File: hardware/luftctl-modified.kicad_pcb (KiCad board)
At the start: 2 copper layers, 56.6 x 43 mm, 45 parts, among them J1 USB_C_Receptacle_USB2.0, J2 UART, J3 I2C, J4 PWM Fan, J5 PWM Fan, J6 Conn_01x08, SW1 Reset, U3 USBLC6-4SC6, U4 ESP32-C3-WROOM-02, U5 CH224K, U6 LMR51420YFDDCR

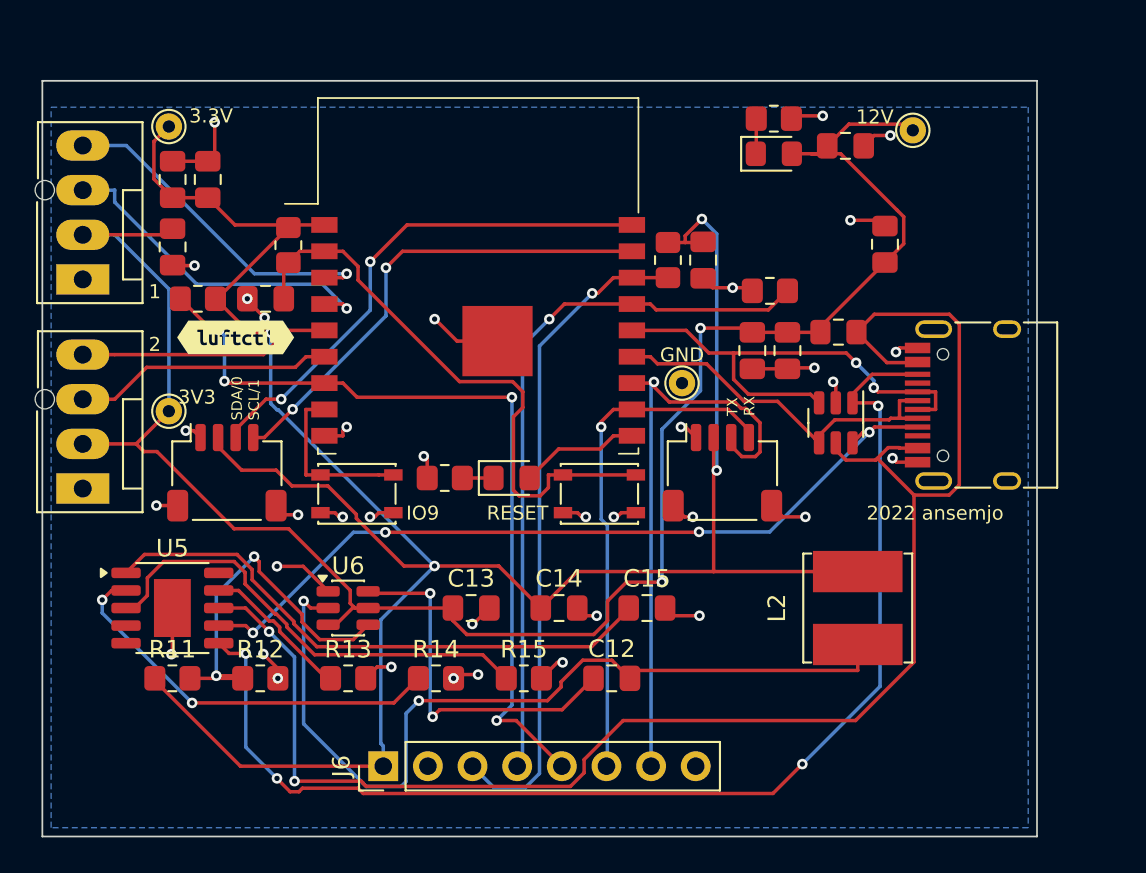
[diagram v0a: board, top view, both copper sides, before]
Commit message: CH224K: fix 12V CFG straps + VDD supply per datasheet; re-route
Datasheet research (WCH CH224 V2.0; TI LMR51420 SLUSEF6C), cross-verified,
corrected two bugs in the CH224K PD-trigger wiring that would have made the
board negotiate 9V with an unpowered controller:

- CFG3 must be pulled HIGH (to VDD) for 12V, not strapped to GND. CH224K has no
  internal CFG pull-ups, so R15 is changed from a 0R GND strap to a 10k pull-up
  to VDD (R15/CFG3 -> VDD_CH). CFG1/CFG2 stay strapped to GND (R13/R14 = 0R):
  CFG1,CFG2,CFG3 = 0,0,1 = 12V.
- VDD (pin 1) needs a series feed from VBUS; add R16 = 1k (VBUS -> VDD_CH) with
  the existing C15 1uF bypass. Previously VDD only had the cap (never powered).

LMR51420 3.3V buck confirmed correct as-is: VREF = 0.6V, R11/R12 = 100k/22k ->
3.327V (in tolerance; TI's exact pair is 100k/22.1k), no feedforward cap.

Board re-synced and re-routed with the corrections (0 unrouted, 0 clearance
violations; remaining DRC items are pre-existing footprint/silk/test-point
issues from the original board). Stale "5V" connector silk corrected to 3V3.
Assembly BOM/CPL and gerbers regenerated (19/27 lines with in-stock LCSC; new
R16 1k = C6654733). Datasheet-confirmed values documented in MODIFICATIONS.md.

Co-Authored-By: Claude Opus 4.8 (1M context) <noreply@anthropic.com>
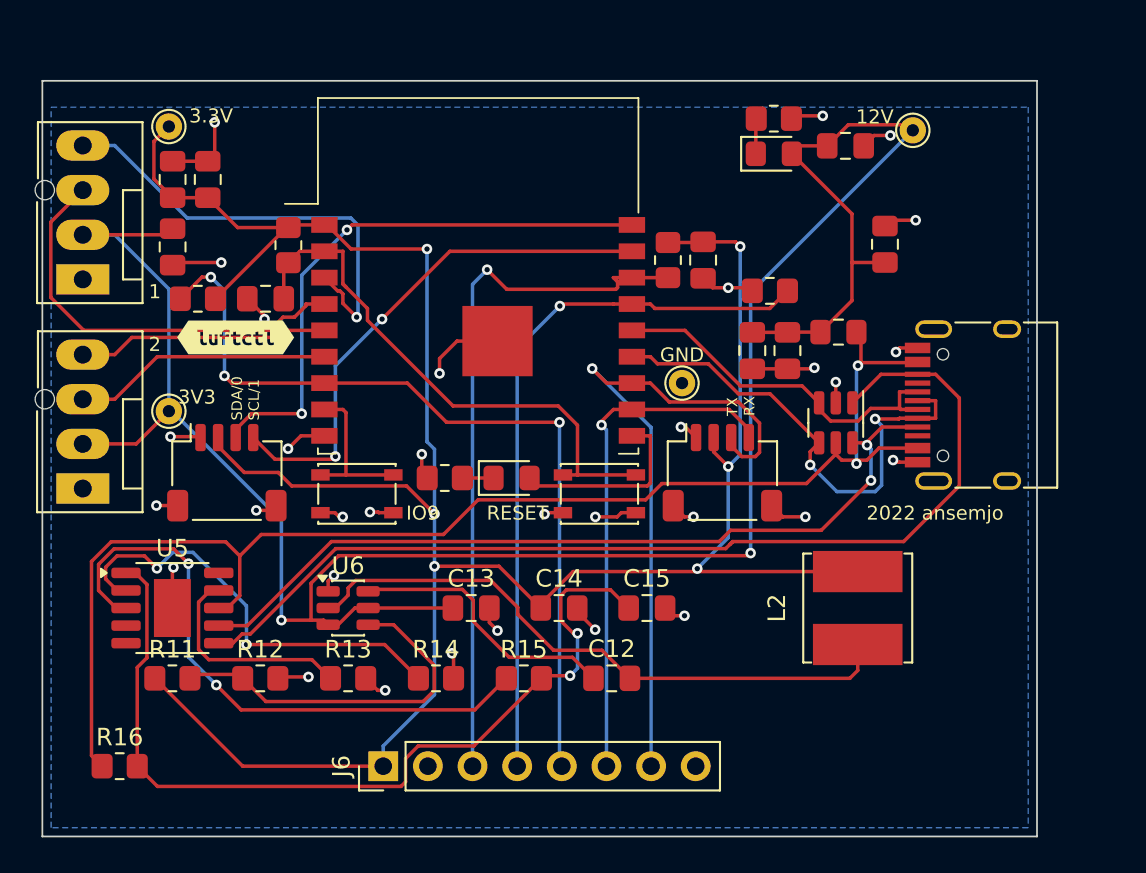
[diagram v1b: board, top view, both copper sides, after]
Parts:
- added R16: 1kΩ, R_0805_2012Metric_Pad1.20x1.40mm_HandSolder, F.Cu at (130.0, 88.0)
- R15: value 0Ω -> 10kΩ
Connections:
- R15 pad 2: GND -> VDD_CH
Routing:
- net +12V: track 108.4 -> 130.4 mm
- net VDD_CH: track 32.6 -> 50.2 mm, vias 0 -> 2
- net VBUS: track 92.0 -> 78.1 mm
- net SW_BUCK: track 49.1 -> 35.2 mm, vias 2 -> 0
- net CC2: track 69.2 -> 58.4 mm, vias 4 -> 0
- net CFG3: track 26.5 -> 34.7 mm, vias 0 -> 2
- net USB-: track 21.0 -> 28.4 mm, vias 0 -> 2
- net USB+: track 27.9 -> 20.9 mm, vias 2 -> 0
- net FAN1_PWM: track 19.4 -> 25.9 mm
- net BST_BUCK: track 20.7 -> 15.7 mm, vias 2 -> 0
- net TXD: track 34.5 -> 38.9 mm
- net FAN1_Tacho: track 19.6 -> 23.9 mm, vias 1 -> 0
- net LED: track 6.82 -> 10.9 mm
- net CFG1: track 8.58 -> 12.3 mm
- net SDA: track 29.4 -> 32.4 mm
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
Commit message: Fix USBLC6 on 12V VBUS, add VBUS TVS, switch to JLCPCB Basic parts
- U3 (USBLC6) pin 5 disconnected from VBUS. VBUS is 12V after PD
  negotiation and the USBLC6 supply-pin clamp conducts from ~6V. Left
  floating (not +3V3) since CC1/CC2 on U3 sit near 5V.
- Add D4 SMF15A (15V standoff) TVS from VBUS to GND, above J1.
- SW1/JP1 buttons: PTS810 -> TS-1088-AR02016 (C720477, JLCPCB Basic).
- Re-source all passives/LEDs to JLCPCB Basic parts; R9 660R -> 680R.
- U4 -> ESP32-C3-WROOM-02-N4 (C2934560, PCB antenna, in stock).
- Pin headers J4/J5/J6 dropped from the assembly BOM (hand-soldered).
- Local re-route; DRC 0 unconnected, no shorts; board matches schematic.
- MODIFICATIONS.md: sourcing notes, order plan, to-do list.

Co-Authored-By: Claude Opus 5.5 (1M context) <noreply@anthropic.com>
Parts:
- added D4: SMF15A, D_SOD-123F, F.Cu at (179.0, 58.4)
- JP1, SW1: footprint Button_Switch_SMD:SW_SPST_PTS810 -> SW_SPST_TS-1088-xR020
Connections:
- U3 pad 5: VBUS -> (no net)
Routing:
- net VBUS: track 78.1 -> 87.7 mm, vias 2 -> 3
- net EN: track 31.7 -> 35.4 mm
- net BOOT: track 9.00 -> 6.59 mm
- net LED: track 10.9 -> 8.51 mm
- net USB-: track 28.4 -> 30.2 mm
- net +3V3: track 138.5 -> 140.2 mm, vias 6 -> 7
- net GND: track 61.2 -> 62.5 mm, vias 32 -> 31
- net VDD_CH: track 50.2 -> 51.0 mm
- net CC1: track 46.9 -> 47.2 mm, vias 2 -> 0

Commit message: Fix TP2 silkscreen: 12V, not 3V3
TP2 is on the +12V rail (the old +5V rail became +12V with the PD input),
but its label had been changed to "3V3".

Co-Authored-By: Claude Opus 5.5 (1M context) <noreply@anthropic.com>
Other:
- board text removed: "3V3"
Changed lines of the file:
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@@
 		)
 	)
-	(gr_text "3V3"
+	(gr_text "12V"
 		(at 134.4 67 0)
 		(layer "F.SilkS")

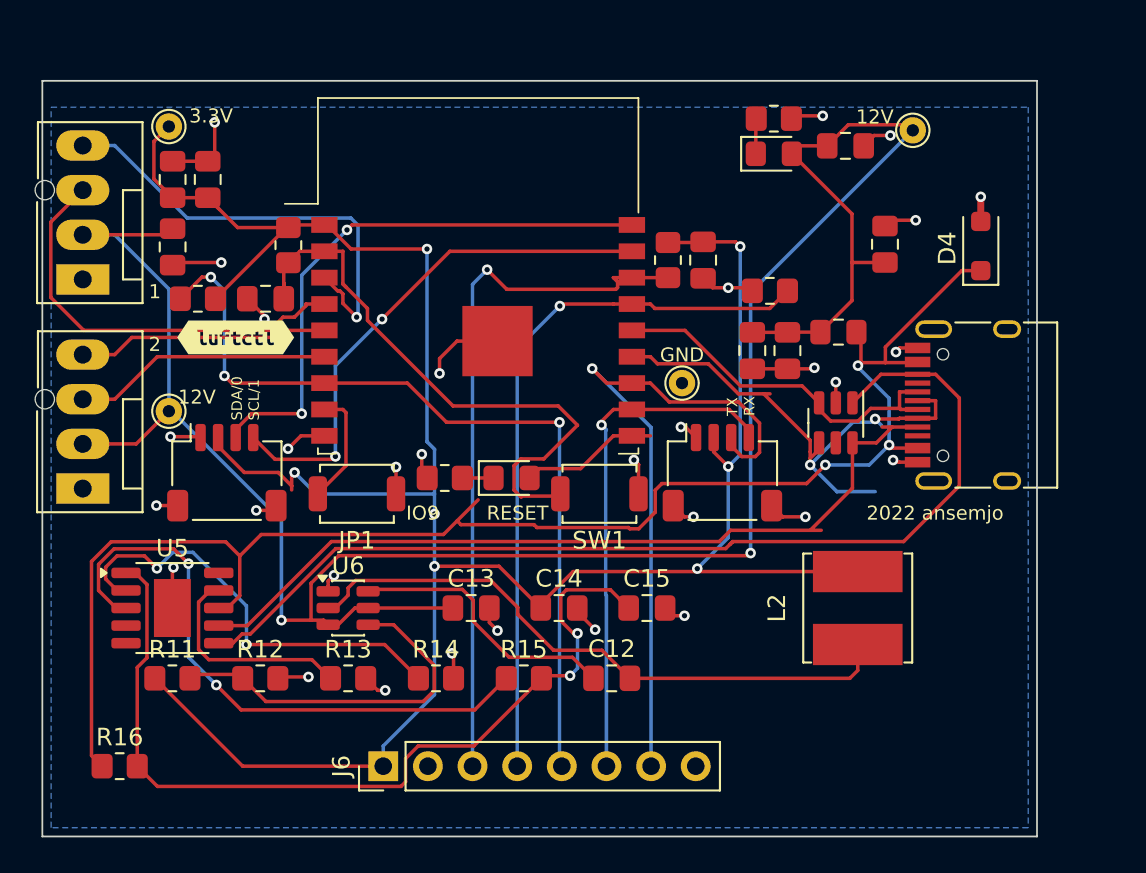
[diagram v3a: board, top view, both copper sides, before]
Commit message: Remove J2/J3 JST-SH connectors; J6 becomes 1x10 with SDA/SCL and pin labels
UART was already on J6 and flashing/logs go over native USB, so J2 was
redundant. SDA (GPIO0) and SCL (GPIO1) move from J3 to J6 pins 9/10.
J6: 3V3, GND, IO2, IO3, IO8, RX, TX, GND, SDA, SCL, labelled on silk.
Local re-route; DRC 0 unconnected, no new violations; board matches
schematic. Drops the C160404 Extended line from the BOM.

Co-Authored-By: Claude Opus 5.5 (1M context) <noreply@anthropic.com>
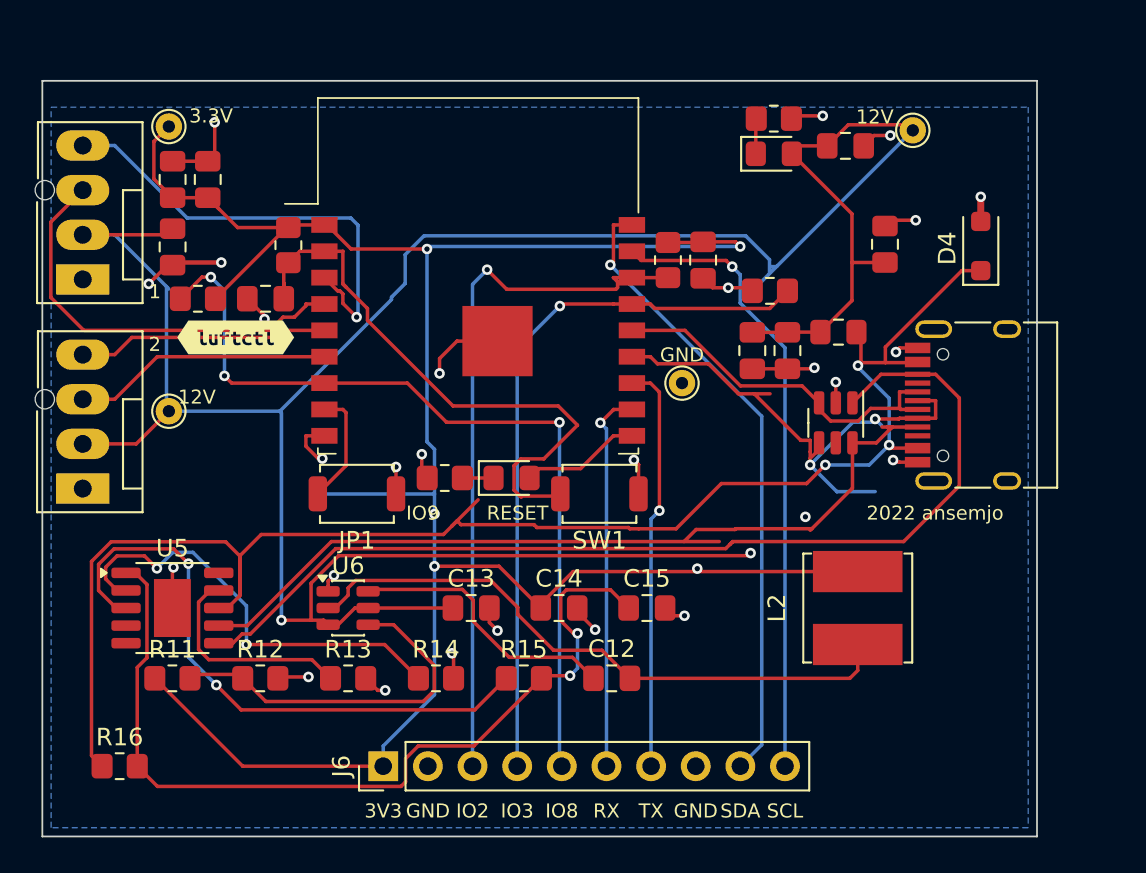
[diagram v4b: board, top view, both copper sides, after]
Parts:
- removed J2: UART, Connector_JST:JST_SH_SM04B-SRSS-TB_1x04-1MP_P1.00mm_Horizontal
- removed J3: I2C, Connector_JST:JST_SH_SM04B-SRSS-TB_1x04-1MP_P1.00mm_Horizontal
- J6: value Conn_01x08 -> Conn_01x10; footprint PinHeader_1x08_P2.54mm_Vertical -> PinHeader_1x10_P2.54mm_Vertical
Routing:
- net +12V: track 130.4 -> 154.2 mm
- net TXD: track 38.9 -> 23.3 mm
- net +3V3: track 140.2 -> 128.3 mm, vias 7 -> 5
- net RXD: track 29.4 -> 21.8 mm
- net SCL: track 30.0 -> 35.7 mm, vias 2 -> 1
- net GND: track 62.5 -> 57.7 mm, vias 31 -> 27
- net SDA: track 32.4 -> 36.0 mm, vias 2 -> 1
- net VBUS: track 87.7 -> 89.7 mm
- net CC1: track 47.2 -> 49.1 mm
- net USB-: track 30.2 -> 31.2 mm
- net LED: track 8.51 -> 7.46 mm
- net EN: track 35.4 -> 36.4 mm
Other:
- board text added: "3V3"
- board text added: "IO2"
- board text added: "IO3"
- board text added: "IO8"
- board text added: "RX"
- board text added: "SCL"
- board text added: "SDA"
- board text added: "TX"
- board text removed: "SDA/0 SCL/1"
- board text removed: "TX RX"

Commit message: Compact layout: 56.7 x 32.1 mm, centred on fan headers and USB-C
- Outline centred on the fan headers (y 62.45); J1 moved down 5 mm to match.
- J6 along the bottom edge; buck and CH224K groups packed beside SW1 and
  under J1; D4/R16 above J1. TP1/TP4 removed.
- GND poured on both layers with via stitching; antenna keep-out extended.
- Re-routed; DRC 0 unconnected, no new violations; board matches schematic.
- CPL regenerated with JLCPCB rotation corrections; gerbers regenerated.

Co-Authored-By: Claude Opus 5.5 (1M context) <noreply@anthropic.com>
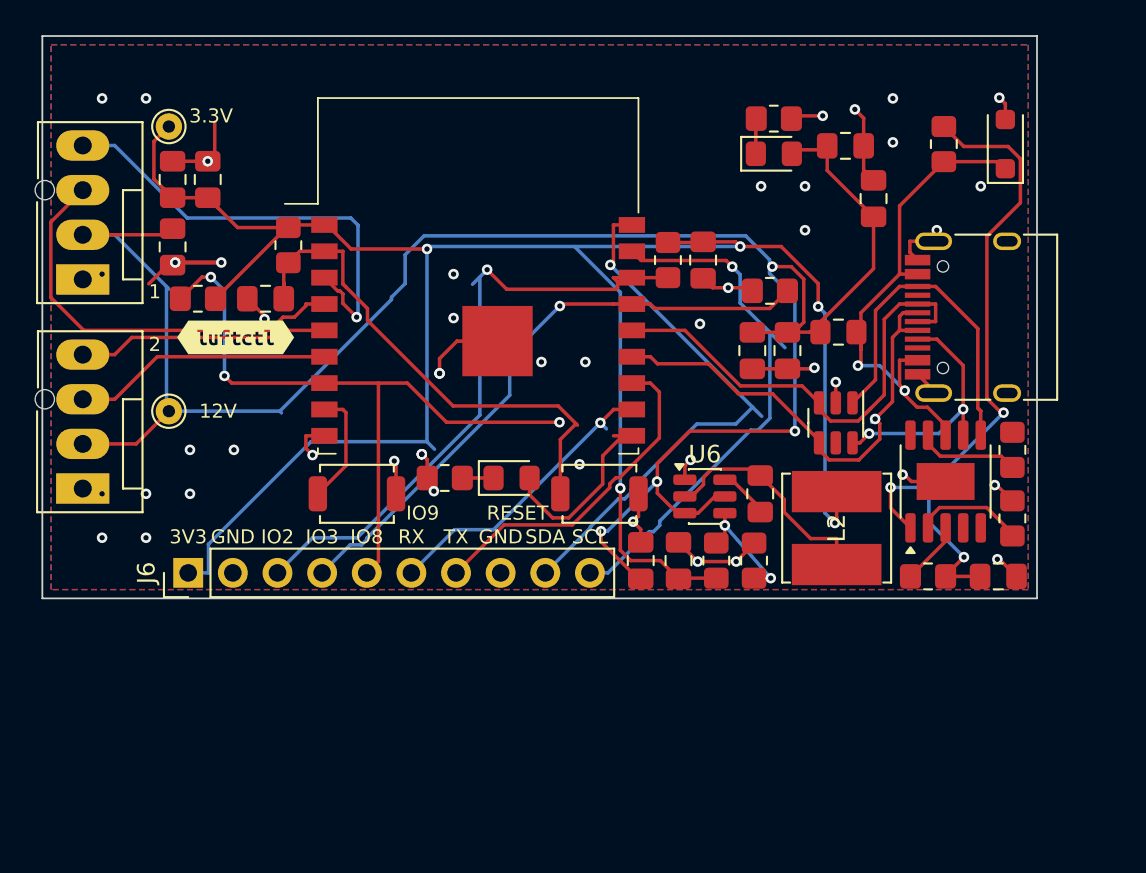
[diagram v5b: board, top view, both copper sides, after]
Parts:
- removed TP1, TP4: Test, TestPoint:TestPoint_THTPad_D1.5mm_Drill0.7mm
- moved R16 58.8 mm to (176.9, 52.6), turned to 90 degrees
- moved U5 44.6 mm to (177.0, 71.8), turned to 90 degrees
- moved R13 40.0 mm to (180.8, 70.0), turned to 90 degrees
- moved R14 34.0 mm to (180.8, 73.9), turned to 90 degrees
- moved R11 31.7 mm to (163.9, 76.3), turned to 90 degrees
- moved R12 28.9 mm to (166.1, 76.3), turned to 90 degrees
- moved R15 23.7 mm to (176.0, 77.2)
- moved U6 21.3 mm to (163.3, 72.7)
- moved C15 20.1 mm to (180.0, 77.2)
- moved J6 15.6 mm to (133.9, 77.0)
- moved C12 13.5 mm to (166.4, 72.5), turned to 90 degrees
- moved C13 10.0 mm to (159.7, 76.3), turned to 90 degrees
- moved C14 7.32 mm to (161.8, 76.3), turned to 90 degrees
- moved D4 5.97 mm to (180.4, 52.6)
- moved J1 5.00 mm to (179.4, 62.5)
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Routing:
- net VBUS: track 89.7 -> 29.5 mm, vias 3 -> 2
- net CC2: track 58.4 -> 19.5 mm
- net CC1: track 49.1 -> 14.3 mm, vias 0 -> 2
- net +12V: track 154.2 -> 123.1 mm, vias 2 -> 4
- net CFG3: track 34.7 -> 3.59 mm, vias 2 -> 0
- net SW_BUCK: track 35.2 -> 13.1 mm
- net CFG2: track 25.6 -> 6.33 mm, vias 2 -> 0
- net FB_BUCK: track 21.1 -> 6.83 mm, vias 0 -> 2
- net BST_BUCK: track 15.7 -> 2.90 mm
- net VDD_CH: track 51.0 -> 40.1 mm, vias 2 -> 3
- net GPIO8: track 48.1 -> 39.4 mm
- net CFG1: track 12.3 -> 5.85 mm
- net USB+: track 20.9 -> 27.3 mm
- net RXD: track 21.8 -> 16.9 mm
- net GPIO3: track 40.7 -> 35.8 mm
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- added copper zone on F.Cu, net GND
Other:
- board size 56.6 x 43 mm -> 56.6 x 32 mm

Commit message: Back silkscreen: 2026 elbob
Co-Authored-By: Claude Opus 5.5 (1M context) <noreply@anthropic.com>
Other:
- board text added: "2026 elbob"
- board text removed: "2022 ansemjo"
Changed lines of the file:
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@@
 		)
 	)
-	(gr_text "2022 ansemjo"
-		(at 160 74 0)
+	(gr_text "2026 elbob"
+		(at 163 73 0)
 		(layer "B.SilkS")
 		(effects
